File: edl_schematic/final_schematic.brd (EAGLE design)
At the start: 283.2 x 286.7 mm, 290 parts, among them IC1 FT232RL, IC10 TL084D, IC11 TL084D, IC12 TL084D, IC13 TL084D, IC14 TL084D, IC15 TL084D, IC16 TL084D, IC17 TL084D, IC18 TL084D, IC19 TL084D, IC2 TL084D, IC20 TL084D, IC21 TL084D, IC22 TL084D, IC23 TL084D, IC24 TL084D, IC3 TL084D, IC4 TPS77333, IC6 7812TV, IC8 TL084D, IC9 TL084D, Q1 BC558B, U1 TMS320F28069_PN_80, U3 TLV5610_DW_20, U4 MAX395EWG, U6 MAX395EWG, U7 MAX395EWG

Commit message: small schematic added
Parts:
- removed R1, R197: (no value), SparkFun-Resistors:1206
- added JP19, JP20, JP21, JP22: (no value), jumper:JP4
- moved C38 520.8 mm to (345.6, -126.6), turned to 180 degrees
- moved R156 467.3 mm to (345.6, -130.8), turned to 180 degrees
- moved R168 464.2 mm to (248.7, -127.4), turned to 180 degrees
- moved R152 463.1 mm to (345.6, -100.2), turned to 180 degrees
- moved R167 462.2 mm to (262.5, -112.8), turned to 0 degrees
- moved R151 456.7 mm to (319.7, -103.6), turned to 180 degrees
- moved C41 454.6 mm to (240.8, -123.6), turned to 0 degrees
- moved C42 453.1 mm to (249.0, -123.4), turned to 180 degrees
- moved R153 452.1 mm to (319.9, -110.8), turned to 180 degrees
- moved R155 450.1 mm to (320.5, -120.6), turned to 180 degrees
- moved R154 449.0 mm to (337.6, -101.2), turned to 0 degrees
- moved C39 440.2 mm to (240.6, -97.8), turned to 0 degrees
- moved C40 439.0 mm to (249.1, -97.6), turned to 180 degrees
- moved R140 437.7 mm to (345.6, -123.1), turned to 0 degrees
- moved R139 430.5 mm to (345.5, -107.7), turned to 0 degrees
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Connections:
- removed net A3Q\: U4.8
- removed net DTR_OUT: Q1.C, R1.2, R197.2
- new net INTEG_IN11: JP22.1, R144.1, R145.1
- new net INTEG_IN22: JP22.2, R155.1, R156.1
- new net INTEG_IN33: JP22.3, R151.1, R152.1
- new net INTEG_IN44: JP22.4, R153.1, R154.1
- new net INTEG_IN55: JP21.1, R161.1, R162.1
- new net INTEG_IN66: JP21.2, R167.1, R168.1
- new net INTEG_IN77: JP21.3, R163.1, R164.1
- new net INTEG_IN88: JP21.4, R165.1, R166.1
- net 3V3: now also IC4.1, IC4.2; no longer Q1.E
- net A1P: now also U4.8; no longer U4.5
- net A1Q: now also U4.7; no longer U4.6
- net A3P: now also R155.2, U4.5; no longer R151.2, U4.7
- net A3Q: now also C38.2, IC23.6, R140.1, R156.2, U4.6; no longer C36.2, IC23.9, R139.1, R152.2
- net A5P: now also R151.2, U4.12; no longer R155.2, U4.9
- net A5Q: now also C36.2, IC23.9, R139.1, R152.2, U4.11; no longer C38.2, IC23.6, R140.1, R156.2, U4.10
- net A7P: now also U4.9; no longer U4.11
- net A7Q: now also U4.10; no longer U4.12
- net B1P: now also U4.20; no longer U4.14
- net B1Q: now also U4.19; no longer U4.13
- net B3P: now also R167.2, U4.17; no longer R163.2, U4.16
- net B3Q: now also C42.2, IC24.6, R158.1, R168.2, U4.18; no longer C40.2, IC24.9, R157.1, R164.2, U4.15
- net B5P: now also R163.2, U4.16; no longer R167.2, U4.18
- net B5Q: now also C40.2, IC24.9, R157.1, R164.2, U4.15; no longer C42.2, IC24.6, R158.1, R168.2, U4.17
- net B7P: now also U4.13; no longer U4.20
- net B7Q: now also U4.14; no longer U4.19
- net GND: now also IC4.3, Q1.C; no longer R197.1
- net INTEG_IN1: now also JP19.4; no longer R144.1, R145.1
- net INTEG_IN2: now also JP19.3; no longer R155.1, R156.1
- net INTEG_IN3: now also JP19.2; no longer R151.1, R152.1
- net INTEG_IN4: now also JP19.1; no longer R153.1, R154.1
- net INTEG_IN5: now also JP20.4; no longer R161.1, R162.1
- net INTEG_IN6: now also JP20.3; no longer R167.1, R168.1
- net INTEG_IN7: now also JP20.2; no longer R163.1, R164.1
- net INTEG_IN8: now also JP20.1; no longer R165.1, R166.1
- net RST_OUT: now also Q1.E; no longer R1.1
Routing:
- net N$65: track 17.1 -> 127.0 mm
- net A3Q: track 0.00 -> 89.7 mm
- net INTEG_IN1: track 0.12 -> 85.9 mm
- net A1Q: track 0.00 -> 83.5 mm
- net INTEG_IN4: track 5.54 -> 87.5 mm
- net INTEG_IN22: track 0.00 -> 78.3 mm
- net B1Q: track 0.00 -> 77.4 mm
- net B7Q: track 0.00 -> 76.6 mm
- net A5Q: track 0.00 -> 73.9 mm
- net +3.3V: track 73.1 -> 0.00 mm
- net B3Q: track 0.00 -> 71.6 mm
- net B5Q: track 0.00 -> 70.6 mm
- net A7Q: track 0.00 -> 70.3 mm
- net INTEG_IN33: track 0.00 -> 68.5 mm
- net INTEG_IN88: track 0.00 -> 64.5 mm
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
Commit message: Small board done except power and switch
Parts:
- removed IC10, IC11, IC12, IC13, IC2, IC8, IC9: TL084D, linear:SO14
- removed R12: (no value), resistor:0207/7
- removed R18, R19, R20, R21, R22, R23, R24, R25, R35, R36, R37, R38, R39, R40, R41, R42, R43, R44, R45, R46, R47, R48, R49, R50, R51, R52, R53, R54, R55, R56, R57, R58, R59, R60, R61, R62, R63, R64, R65, R66, R67, R68, R69, R70, R71, R72, R73, R74, R75, R76, R77, R78, R79, R80, R81, R82, R83, R84, R85, R86, R87, R88: (no value), rcl:R1206
- added IC25, IC26, IC27, IC28, IC29, IC30, IC5: TL084D, linear:SO14
- added JP24, JP25: (no value), jumper:JP4
- added R1, R14, R197, R198, R199, R200, R201, R202, R203, R204, R205, R206, R207, R208, R209, R210, R211, R212, R213, R214, R215, R216, R217, R218, R219, R220, R221, R222, R223, R224, R225, R226, R227, R228, R229, R230, R231, R232, R233, R234, R235, R236, R237, R238, R239, R240, R241, R242, R243, R244, R245, R246, R247, R248, R249, R250, R251, R252, R253, R254, R255, R5, R6: (no value), rcl:R1206
- R10, R11, R8, R9: device resistor:0207/7 -> rcl:R1206
- moved JP2 302.3 mm to (8.13, 29.4), turned to 180 degrees
- moved JP3 264.5 mm to (54.8, 72.5), turned to 270 degrees
- moved R11 256.3 mm to (43.0, 60.5)
- moved JP10 254.8 mm to (43.2, 53.8)
- moved JP7 253.2 mm to (46.8, 53.7), turned to 270 degrees
- moved R10 253.2 mm to (44.1, 45.0), turned to 270 degrees
- moved R9 250.9 mm to (46.6, 60.4)
- moved JP11 246.7 mm to (50.7, 53.6)
- moved R8 246.6 mm to (50.6, 60.4), turned to 270 degrees
- moved JP5 243.5 mm to (54.7, 78.2)
- moved C22 240.0 mm to (19.1, -3.31), turned to 0 degrees
- moved IC3 221.4 mm to (122.7, 37.1)
- moved R17 219.1 mm to (47.5, 45.0), turned to 270 degrees
- moved R7 217.6 mm to (27.5, -3.15), turned to 0 degrees
- moved U7 214.7 mm to (178.7, -6.26), turned to 90 degrees
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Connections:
- removed net +3.3V: R104.1, R110.1, R116.1, R122.1, R128.1, R134.1, R22.1, R31.1, R40.1, R49.1, R58.1, R67.1, R76.1, R85.1, R92.1, R98.1
- removed net 5V: U6.2, U6.23, U7.2, U7.23
- removed net N$22: IC2.2, R17.2, R18.1
- removed net N$24: IC2.1, R18.2, R19.1
- removed net N$25: IC2.9, R19.2, R20.1
- removed net N$27: IC2.8, R20.2, R21.1
- removed net N$29: IC2.7, R23.1, R25.2
- removed net N$34: IC2.13, R23.2, R24.1
- removed net N$35: IC2.6, R21.2, R22.2, R25.1
- removed net N$44: IC8.2, R35.2, R36.1
- removed net N$45: IC8.1, R36.2, R37.1
- removed net N$46: IC8.9, R37.2, R38.1
- removed net N$47: IC8.8, R38.2, R39.1
- removed net N$48: IC8.7, R41.1, R43.2
- removed net N$50: IC8.13, R41.2, R42.1
- removed net N$51: IC8.6, R39.2, R40.2, R43.1
- removed net N$52: IC9.2, R44.2, R45.1
- removed net N$53: IC9.1, R45.2, R46.1
- removed net N$54: IC9.9, R46.2, R47.1
- removed net N$55: IC9.8, R47.2, R48.1
- removed net N$56: IC9.7, R50.1, R52.2
- removed net N$58: IC9.13, R50.2, R51.1
- removed net N$59: IC9.6, R48.2, R49.2, R52.1
- removed net N$60: IC10.2, R53.2, R54.1
- removed net N$61: IC10.1, R54.2, R55.1
- removed net N$62: IC10.9, R55.2, R56.1
- removed net N$63: IC10.8, R56.2, R57.1
- removed net N$64: IC10.7, R59.1, R61.2
- removed net N$66: IC10.13, R59.2, R60.1
- removed net N$67: IC10.6, R57.2, R58.2, R61.1
- removed net N$68: IC11.2, R62.2, R63.1
- removed net N$69: IC11.1, R63.2, R64.1
- removed net N$70: IC11.9, R64.2, R65.1
- removed net N$71: IC11.8, R65.2, R66.1
- removed net N$72: IC11.7, R68.1, R70.2
- removed net N$74: IC11.13, R68.2, R69.1
- removed net N$75: IC11.6, R66.2, R67.2, R70.1
- removed net N$76: IC12.2, R71.2, R72.1
- removed net N$77: IC12.1, R72.2, R73.1
- removed net N$78: IC12.9, R73.2, R74.1
- removed net N$79: IC12.8, R74.2, R75.1
- removed net N$80: IC12.7, R77.1, R79.2
- removed net N$82: IC12.13, R77.2, R78.1
- removed net N$83: IC12.6, R75.2, R76.2, R79.1
- removed net N$84: IC13.2, R80.2, R81.1
- removed net N$85: IC13.1, R81.2, R82.1
- removed net N$86: IC13.9, R82.2, R83.1
- removed net N$87: IC13.8, R83.2, R84.1
- removed net N$88: IC13.7, R86.1, R88.2
- removed net N$90: IC13.13, R86.2, R87.1
- removed net N$91: IC13.6, R84.2, R85.2, R88.1
- new net N$134: IC5.1, R5.2, R6.1
- new net N$135: IC3.7, R29.2, R30.1
- new net N$137: IC5.6, R14.1, R6.2
- new net N$138: IC5.8, R199.1, R201.2
- new net N$139: IC5.13, R199.2, R200.1
- new net N$140: IC5.9, R197.2, R198.2, R201.1
- new net N$141: IC5.7, R14.2, R197.1
- new net N$142: IC25.2, R202.2, R203.1
- new net N$143: IC25.1, R203.2, R204.1
- new net N$144: IC25.6, R204.2, R205.1
- new net N$145: IC25.8, R208.1, R210.2
- new net N$146: IC25.13, R208.2, R209.1
- new net N$147: IC25.9, R206.2, R207.2, R210.1
- new net N$148: IC25.7, R205.2, R206.1
- new net N$149: IC26.2, R211.2, R212.1
- new net N$150: IC26.1, R212.2, R213.1
- new net N$151: IC26.6, R213.2, R214.1
- new net N$152: IC26.8, R217.1, R219.2
- new net N$153: IC26.13, R217.2, R218.1
- new net N$154: IC26.9, R215.2, R216.2, R219.1
- new net N$155: IC26.7, R214.2, R215.1
- new net N$156: IC27.2, R220.2, R221.1
- new net N$157: IC27.1, R221.2, R222.1
- new net N$158: IC27.6, R222.2, R223.1
- new net N$159: IC27.8, R226.1, R228.2
- new net N$160: IC27.13, R226.2, R227.1
- new net N$161: IC27.9, R224.2, R225.2, R228.1
- new net N$162: IC27.7, R223.2, R224.1
- new net N$163: IC28.2, R229.2, R230.1
- new net N$164: IC28.1, R230.2, R231.1
- new net N$165: IC28.6, R231.2, R232.1
- new net N$166: IC28.8, R235.1, R237.2
- new net N$167: IC28.13, R235.2, R236.1
- new net N$168: IC28.9, R233.2, R234.2, R237.1
- new net N$169: IC28.7, R232.2, R233.1
- new net N$170: IC29.2, R238.2, R239.1
- new net N$171: IC29.1, R239.2, R240.1
- new net N$172: IC29.6, R240.2, R241.1
- new net N$173: IC29.8, R244.1, R246.2
- new net N$174: IC29.13, R244.2, R245.1
- new net N$175: IC29.9, R242.2, R243.2, R246.1
- new net N$176: IC29.7, R241.2, R242.1
- new net N$177: IC30.2, R247.2, R248.1
- new net N$178: IC30.1, R248.2, R249.1
- new net N$179: IC30.6, R249.2, R250.1
- new net N$180: IC30.8, R253.1, R255.2
- new net N$181: IC30.13, R253.2, R254.1
- new net N$182: IC30.9, R251.2, R252.2, R255.1
- new net N$183: IC30.7, R250.2, R251.1
- net +12V: now also IC25.4, IC26.4, IC27.4, IC28.4, IC29.4, IC30.4, IC5.4, U4.2, U4.23, U6.2, U6.23, U7.2, U7.23; no longer IC10.4, IC11.4, IC12.4, IC13.4, IC2.4, IC8.4, IC9.4
- net -12V: now also IC25.11, IC26.11, IC27.11, IC28.11, IC29.11, IC30.11, IC5.11; no longer IC10.11, IC11.11, IC12.11, IC13.11, IC2.11, IC8.11, IC9.11
- net 3V3: now also R104.1, R110.1, R116.1, R122.1, R128.1, R134.1, R198.1, R207.1, R216.1, R225.1, R234.1, R243.1, R252.1, R31.1, R9.2, R92.1, R98.1; no longer R12.2, U4.2, U4.23
- net ADC_IN1: now also IC30.14, JP25.4, R254.2; no longer IC3.14, JP18.1, R33.2
- net ADC_IN2: now also IC28.14, JP25.3, R236.2; no longer IC11.14, JP18.3, R69.2
- net ADC_IN3: now also IC26.14, JP25.2, R218.2; no longer IC8.14, JP18.5, R42.2
- net ADC_IN4: now also IC25.14, JP25.1, R209.2; no longer IC12.14, JP18.7, R78.2
- net ADC_IN5: now also IC3.14, JP24.1, R33.2; no longer IC9.14, JP18.9, R51.2
- net ADC_IN6: now also IC5.14, JP24.2, R200.2; no longer IC2.14, JP18.11, R24.2
- net ADC_IN7: now also IC27.14, JP24.3, R227.2; no longer IC10.14, JP18.13, R60.2
- net ADC_IN8: now also IC29.14, JP24.4, R245.2; no longer IC13.14, JP18.15, R87.2
- net ADC_ORG1: now also JP18.6; no longer JP18.2
- net ADC_ORG2: now also JP18.8; no longer JP18.4
- net ADC_ORG3: now also JP18.10; no longer JP18.6
- net ADC_ORG4: now also JP18.12; no longer JP18.8
- net ADC_ORG5: now also JP18.14; no longer JP18.10
- net ADC_ORG6: now also JP18.16; no longer JP18.12
- net ADC_ORG7: now also JP18.4; no longer JP18.14
- net ADC_ORG8: now also JP18.2; no longer JP18.16
- net C1Q: now also U6.12, U6.5; no longer JP12.6, U6.6, U6.8
- net C3Q: now also U6.8, U6.9; no longer JP12.8, U6.10, U6.12
- net C5Q: now also JP12.10, JP12.9
- net C7Q: now also JP12.5, JP12.6
- net COMP2: now also R17.2; no longer R8.2
- net D1Q: now also U7.12, U7.5; no longer JP12.5, U7.6, U7.8
- net D3Q: now also U7.8, U7.9; no longer JP12.7, U7.10, U7.12
- net FORCE1: now also JP9.12; no longer JP9.11
- net FORCE2: now also JP9.14; no longer JP9.12
- net FORCE3: now also JP9.11; no longer JP9.13
- net FORCE4: now also JP9.13; no longer JP9.14
- net GND: now also IC25.10, IC25.12, IC25.3, IC25.5, IC26.10, IC26.12, IC26.3, IC26.5, IC27.10, IC27.12, IC27.3, IC27.5, IC28.10, IC28.12, IC28.3, IC28.5, IC29.10, IC29.12, IC29.3, IC29.5, IC30.10, IC30.12, IC30.3, IC30.5, IC5.10, IC5.12, IC5.3, IC5.5, R17.1; no longer IC10.10, IC10.12, IC10.3, IC10.5, IC11.10, IC11.12, IC11.3, IC11.5, IC12.10, IC12.12, IC12.3, IC12.5, IC13.10, IC13.12, IC13.3, IC13.5, IC2.10, IC2.12, IC2.3, IC2.5, IC8.10, IC8.12, IC8.3, IC8.5, IC9.10, IC9.12, IC9.3, IC9.5, JP12.13, JP12.14, R9.1
- net LIN_OUT1: now also JP12.13; no longer JP12.10
- net LIN_OUT1_SW: now also JP12.14; no longer JP12.12
- net LIN_OUT2: now also JP12.1; no longer JP12.9
- net LIN_OUT2_SW: now also JP12.2; no longer JP12.11
- net N$19: now also R9.1; no longer R11.1
- net N$21: now also R11.1; no longer R12.1
- net N$38: now also IC3.6; no longer IC3.9
- net N$39: now also IC5.2, R1.2, R5.1; no longer IC3.8, R29.2, R30.1
- net N$40: now also IC3.8; no longer IC3.7
- net N$43: now also IC3.9; no longer IC3.6
- net TDO: now also R10.2; no longer R9.2
- net TRST: now also R8.2; no longer R10.2
- net U1: now also JP12.11; no longer JP12.2
- net U2: now also JP12.3; no longer JP12.1
- net VIN1: now also R247.1; no longer R26.1, U6.5, U6.9
- net VIN1_INV: now also U6.10; no longer U6.7
- net VIN1_SW: now also JP12.12, U6.6, U6.7; no longer JP12.4
- net VIN2: now also JP15.3, R229.1; no longer JP15.2, R62.1, U7.5, U7.9
- net VIN2_INV: now also U7.6; no longer U7.11
- net VIN2_SW: now also JP12.4, U7.10, U7.11; no longer JP12.3
- net VIN3: now also JP15.5, R211.1; no longer JP15.3, R35.1
- net VIN4: now also JP15.7, R202.1; no longer JP15.4, R71.1
- net VIN5: now also JP15.2, R26.1; no longer JP15.5, R44.1
- net VIN6: now also JP15.4, R1.1; no longer JP15.6, R17.1
- net VIN7: now also JP15.6, R220.1; no longer JP15.7, R53.1
- net VIN8: now also R238.1; no longer R80.1
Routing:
- net +12V: track 72.3 -> 1904.5 mm, vias 0 -> 32
- net -12V: track 23.2 -> 1701.5 mm, vias 0 -> 33
- net 3V3: track 23.6 -> 1513.8 mm, vias 0 -> 35
- net CS_SW: track 0.00 -> 416.4 mm, vias 0 -> 8
- net SPI_CLK_SW: track 0.00 -> 385.4 mm, vias 0 -> 4
- net SPI_MOSI_SW: track 0.00 -> 262.2 mm, vias 0 -> 4
- net CHAN_H1: track 0.00 -> 240.2 mm, vias 0 -> 1
- net CHAN_A1: track 0.00 -> 232.0 mm, vias 0 -> 1
- net GND: track 11.1 -> 235.2 mm, vias 0 -> 27
- net LIN_OUT1_SW: track 0.00 -> 222.1 mm, vias 0 -> 6
- net CHAN_G1: track 0.00 -> 195.0 mm, vias 0 -> 1
- net CHAN_C1: track 0.00 -> 183.4 mm, vias 0 -> 1
- net VIN1: track 9.60 -> 163.3 mm, vias 0 -> 3
- net CHAN_D1: track 0.00 -> 143.2 mm, vias 0 -> 3
- net LIN_OUT2_SW: track 0.00 -> 141.9 mm, vias 0 -> 3
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- added copper zone on layer 1, net GND
- added copper zone on layer 16, net GND
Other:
- board size 283.2 x 286.7 mm -> 486.3 x 283.2 mm

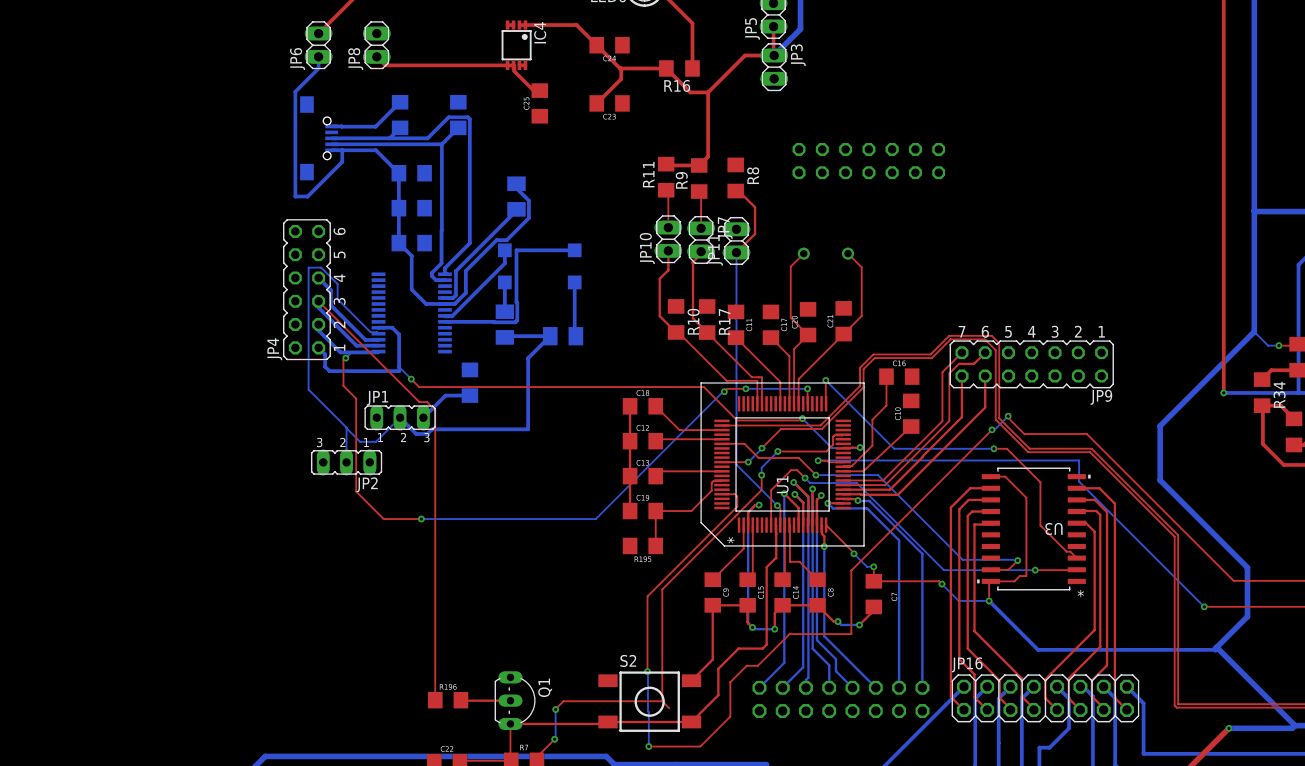
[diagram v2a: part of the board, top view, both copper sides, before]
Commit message: layout done except drc
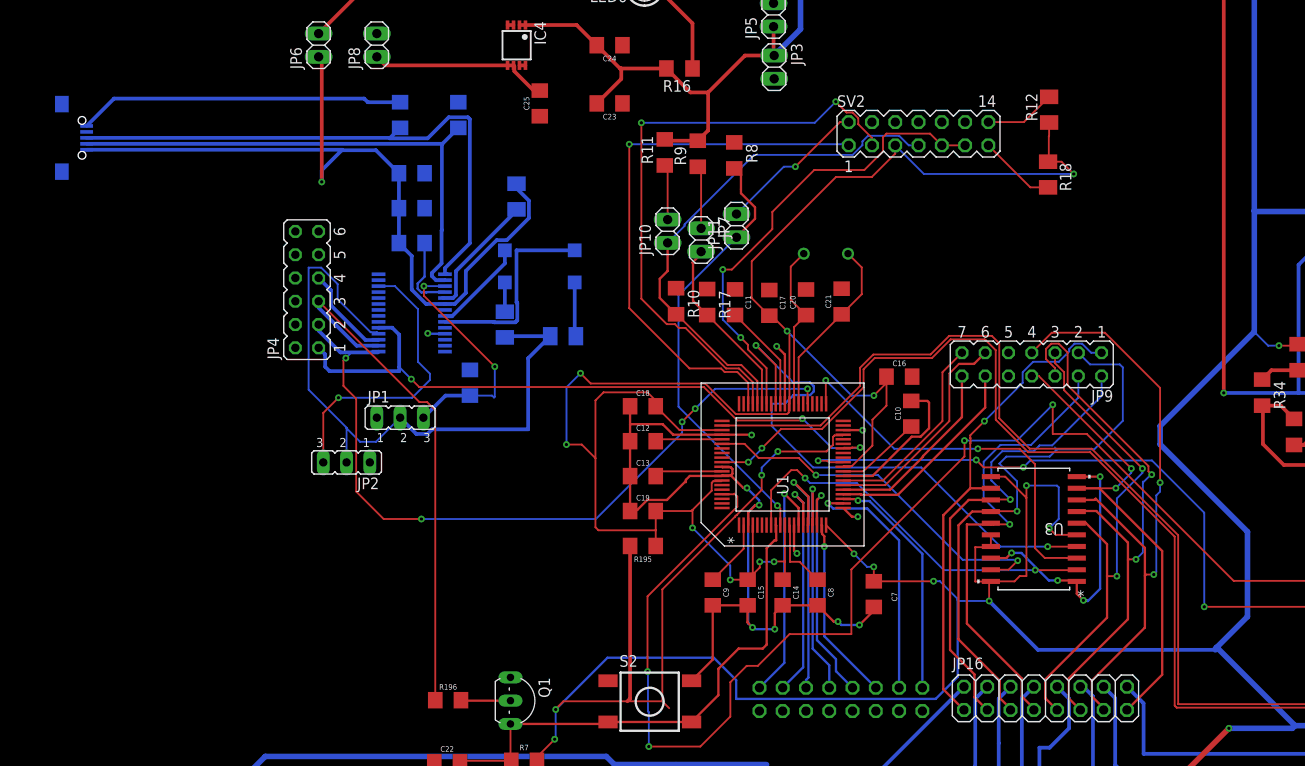
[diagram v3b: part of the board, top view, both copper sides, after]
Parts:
- removed JP14: (no value), jumper:JP7Q
- added R12, R18: 4.7K, rcl:M1206
- added SV2: JTAG, con-lstb:MA07-2
- moved U2 26.7 mm to (-22.9, 64.8)
- moved R11 2.70 mm to (42.8, 63.2)
- moved R9 2.70 mm to (46.4, 63.1)
- moved R8 2.47 mm to (50.4, 62.9)
- moved C11 2.46 mm to (50.5, 46.9)
- moved C17 2.40 mm to (54.3, 46.8)
- moved C20 2.18 mm to (58.3, 46.9)
- moved C21 2.16 mm to (62.1, 47.0)
- moved R10 1.99 mm to (44.1, 47.0)
- moved R17 1.90 mm to (47.5, 46.9)
- moved JP11 1.67 mm to (50.7, 55.2)
- moved JP10 0.88 mm to (43.2, 54.6)
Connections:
- removed net N$12: C14.1, U1.11
- removed net N$13: C15.1, U1.4
- removed net N$136: R195.2
- removed net N$14: C16.1, U1.30
- removed net N$15: C17.2, U1.49
- removed net N$16: C18.2, U1.63
- removed net N$17: C19.2, R195.1, U1.74
- removed net SRST\: JP14.12
- removed net VCCS: JP14.1
- removed net VTREF: JP14.13
- new net N$22: R18.2, SV2.13
- new net N$24: R12.2, SV2.14
- new net SPI_CS: U1.52, U3.4
- new net VDDIO: C14.1, C15.1, C16.1, C17.2, C18.2, C19.2, R12.1, R18.1, R195.1, SV2.5, U1.11, U1.30, U1.4, U1.49, U1.63, U1.74
- net 3V3: now also R195.2, U3.16, U3.17, U3.5
- net GND: now also SV2.10, SV2.12, SV2.4, SV2.8, U3.18; no longer JP14.10, JP14.14, JP14.2, JP14.4, JP14.6, JP14.8
- net JTAG_TRST: now also SV2.2
- net TCK: now also SV2.11, SV2.9; no longer JP14.9
- net TDI: now also SV2.3; no longer JP14.5
- net TDO: now also SV2.7; no longer JP14.11
- net TMS: now also SV2.1; no longer JP14.7
- net TRST: no longer JP14.3
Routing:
- net VDDIO: track 0.00 -> 211.3 mm, vias 0 -> 9
- net GND: track 235.2 -> 366.6 mm, vias 27 -> 38
- net 3V3: track 1513.8 -> 1608.4 mm, vias 35 -> 37
- net TDI: track 0.00 -> 66.4 mm, vias 0 -> 2
- net SPI_CS: track 0.00 -> 62.3 mm, vias 0 -> 2
- net TMS: track 0.00 -> 60.5 mm, vias 0 -> 1
- net TCK: track 0.00 -> 51.7 mm, vias 0 -> 2
- net CHAN_G: track 26.7 -> 69.4 mm, vias 0 -> 2
- net CHAN_F: track 26.0 -> 63.2 mm, vias 0 -> 2
- net CHAN_C: track 25.8 -> 62.6 mm, vias 0 -> 1
- net TDO: track 23.6 -> 56.2 mm
- net CBUS4: track 0.00 -> 32.2 mm, vias 0 -> 1
- net CHAN_E: track 24.7 -> 56.3 mm, vias 0 -> 2
- net CHAN_D: track 25.4 -> 52.2 mm, vias 0 -> 1
- net USBDP: track 36.0 -> 62.8 mm
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
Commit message: drc done
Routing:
- net GND: track 366.6 -> 384.9 mm, vias 38 -> 41
- net +12V: track 1904.5 -> 1894.5 mm
- net C5Q: track 93.3 -> 98.0 mm
- net 3V3: track 1608.4 -> 1612.9 mm
- net N$31: track 15.3 -> 17.5 mm
- net N$122: track 22.5 -> 23.7 mm
- net N$111: track 16.7 -> 17.9 mm
- net INTEG_IN4: track 87.5 -> 88.7 mm
- net N$103: track 14.5 -> 15.6 mm
- net N$49: track 67.2 -> 66.1 mm
- net VIN2: track 123.4 -> 124.2 mm
- net VBUS: track 89.7 -> 90.4 mm
- net N$101: track 63.0 -> 63.6 mm
- net N$168: track 13.4 -> 14.0 mm
- net VIN1: track 163.3 -> 163.9 mm
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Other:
- board size 486.3 x 283.2 mm -> 329.6 x 243.8 mm

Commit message: usb_module added
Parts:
- removed U2: (no value), MicroUSB:USB-MICRO-SMD
- added X1: USB, con-berg:PN61729
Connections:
- net GND: now also X1.4; no longer U2.GND1
- net USBDM: now also X1.2; no longer U2.D-1
- net USBDP: now also X1.3; no longer U2.D+1
- net VBUS: now also X1.1; no longer U2.VBUS1
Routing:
- net GND: track 384.9 -> 353.4 mm
- net VBUS: track 90.4 -> 110.9 mm
- net USBDP: track 63.3 -> 78.6 mm
- net USBDM: track 57.8 -> 68.6 mm
